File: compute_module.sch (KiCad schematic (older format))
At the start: 22 parts, among them Q1 2N7002P.215

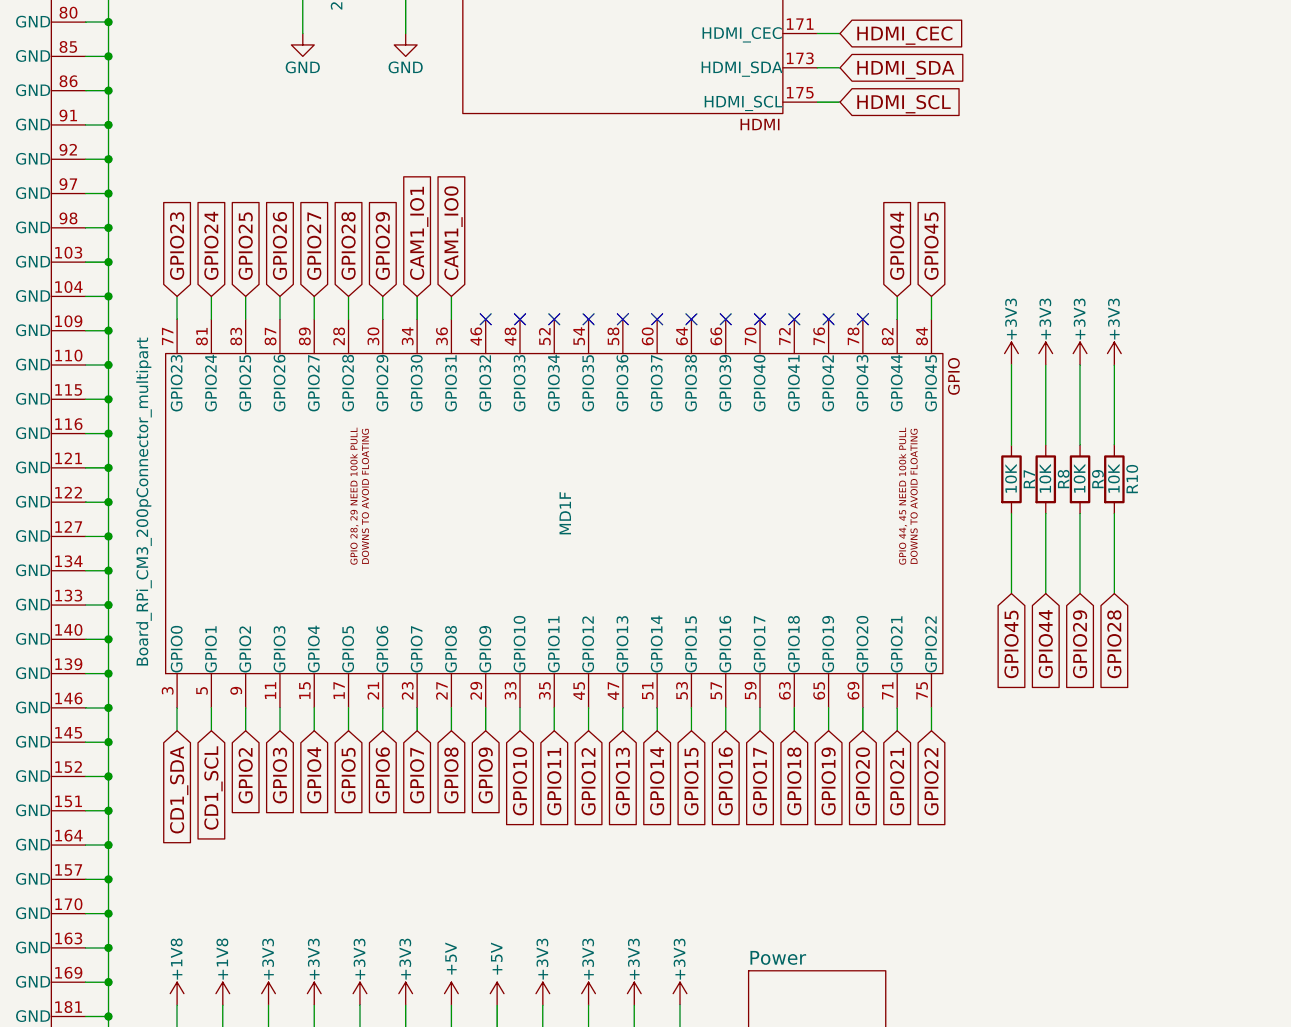
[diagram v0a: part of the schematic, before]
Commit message: Moved camera sda and scl to gpio 28 and 29
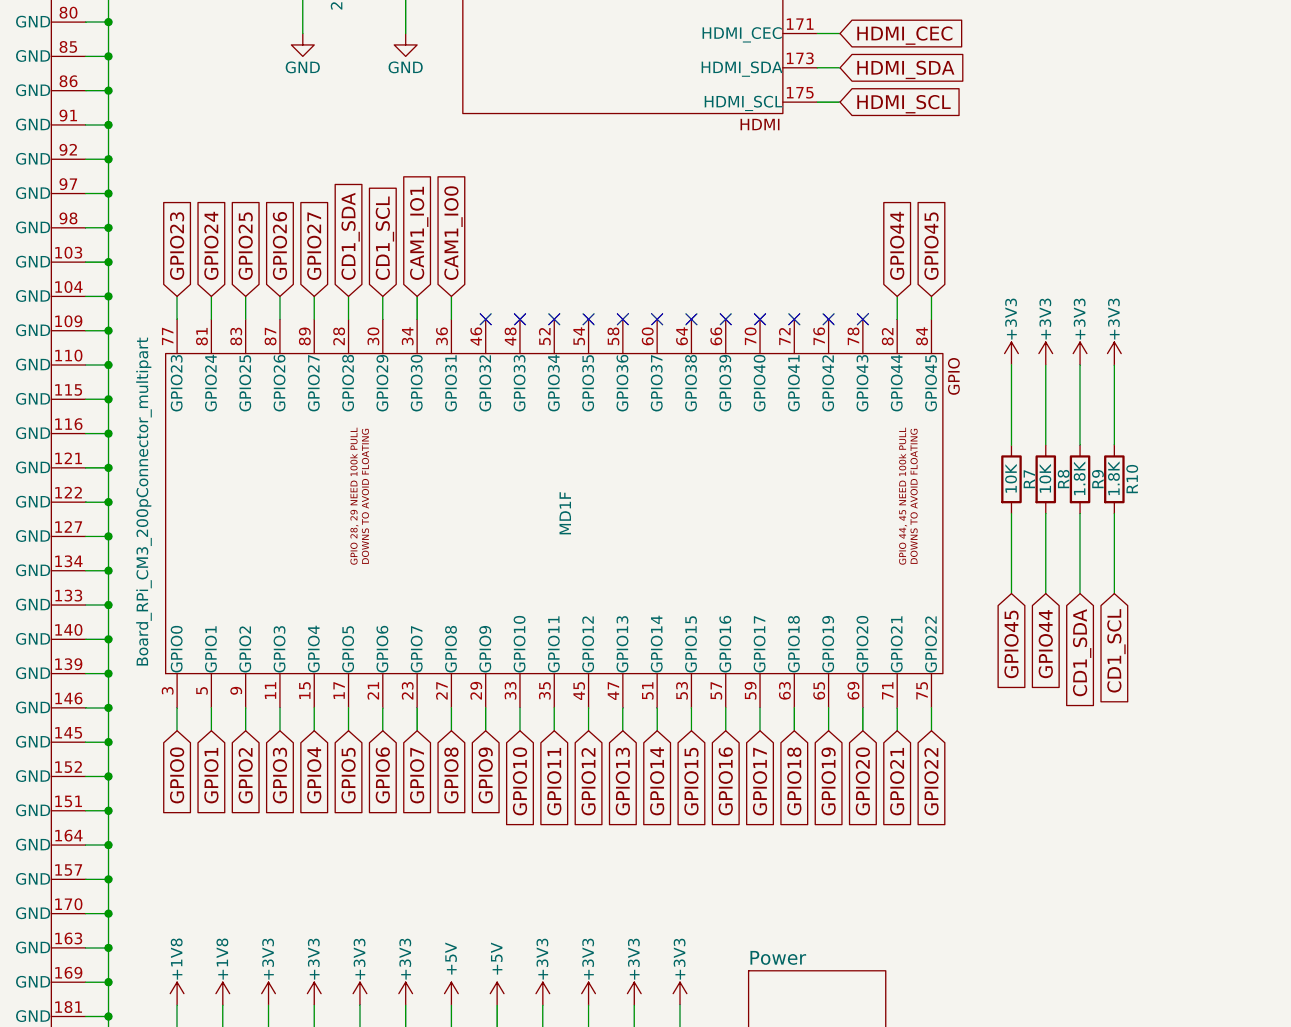
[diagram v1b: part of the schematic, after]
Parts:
- R10, R9: value 10K -> 1.8K
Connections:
- net CD1_SCL: now also MD1.30 (GPIO29), R10.2; no longer MD1.5 (GPIO1)
- net CD1_SDA: now also MD1.28 (GPIO28), R9.2; no longer MD1.3 (GPIO0)
- removed net GPIO28: MD1.28 (GPIO28), R10.2
- removed net GPIO29: MD1.30 (GPIO29), R9.2
- new net GPIO0: MD1.3 (GPIO0)
- new net GPIO1: MD1.5 (GPIO1)
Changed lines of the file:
@@
 NoConn ~ 9150 900
 NoConn ~ 9150 750
-Text GLabel 3550 5450 3    60   Input ~ 0
+Text GLabel 4300 3550 1    60   Input ~ 0
 CD1_SDA
-Text GLabel 3700 5450 3    60   Input ~ 0
+Text GLabel 4450 3550 1    60   Input ~ 0
 CD1_SCL
 Text GLabel 4600 3550 1    60   Input ~ 0
@@
 	1    0    0    -1
 $EndComp
-Text GLabel 4300 3550 1    60   Input ~ 0
-GPIO28
-Text GLabel 4450 3550 1    60   Input ~ 0
-GPIO29
 Text GLabel 6700 3550 1    60   Input ~ 0
 GPIO44
 Text GLabel 6850 3550 1    60   Input ~ 0
 GPIO45
-Text GLabel 7650 4850 3    60   Input ~ 0
-GPIO28
-Text GLabel 7500 4850 3    60   Input ~ 0
-GPIO29
 Text GLabel 7350 4850 3    60   Input ~ 0
 GPIO44
@@
 P 7500 4350
 F 0 "R9" V 7580 4350 50  0000 C CNN
-F 1 "10K" V 7500 4350 50  0000 C CNN
+F 1 "1.8K" V 7500 4350 50  0000 C CNN
 F 2 "Resistors_SMD:R_0603_HandSoldering" V 7430 4350 50  0001 C CNN
 F 3 "" H 7500 4350 50  0000 C CNN
@@
 P 7650 4350
 F 0 "R10" V 7730 4350 50  0000 C CNN
-F 1 "10K" V 7650 4350 50  0000 C CNN
+F 1 "1.8K" V 7650 4350 50  0000 C CNN
 F 2 "Resistors_SMD:R_0603_HandSoldering" V 7580 4350 50  0001 C CNN
 F 3 "" H 7650 4350 50  0000 C CNN
@@
 Text GLabel 4150 3550 1    60   Input ~ 0
 GPIO27
+Text GLabel 7500 4850 3    60   Input ~ 0
+CD1_SDA
+Text GLabel 7650 4850 3    60   Input ~ 0
+CD1_SCL
+Text GLabel 3550 5450 3    60   Input ~ 0
+GPIO0
+Text GLabel 3700 5450 3    60   Input ~ 0
+GPIO1
 $EndSCHEMATC

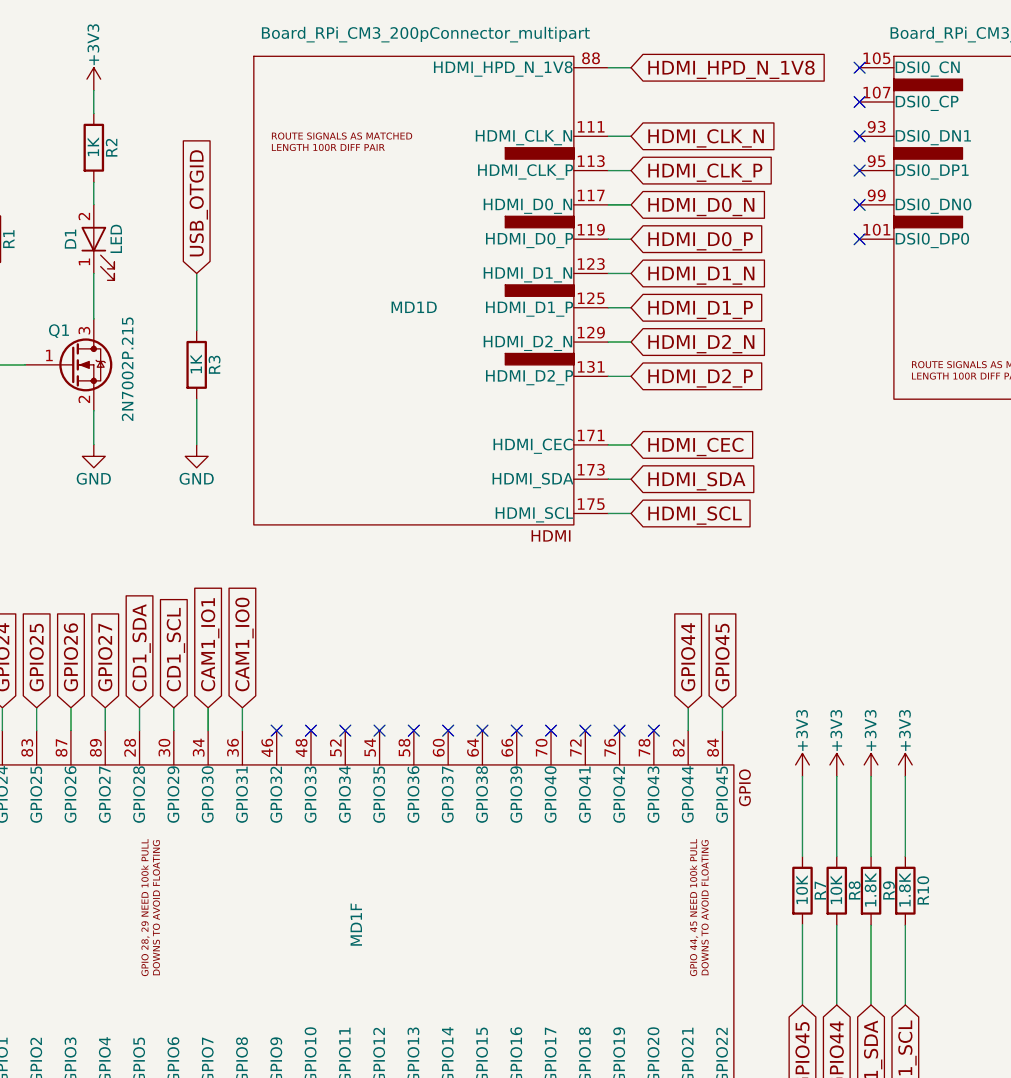
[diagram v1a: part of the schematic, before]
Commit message: Added power LED
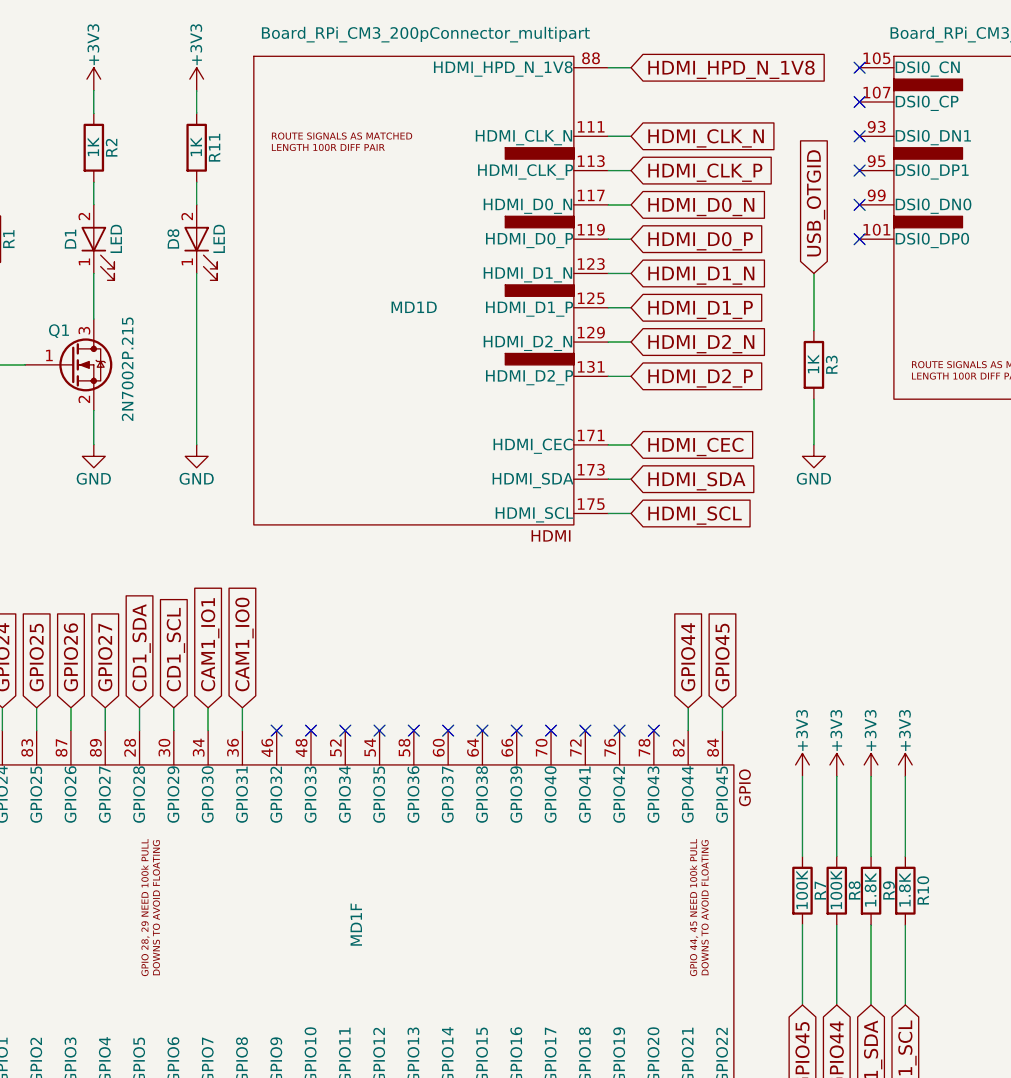
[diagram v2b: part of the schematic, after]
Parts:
- added D8: LED, LEDs:LED_0805, symbol LED
- added R11: 1K, Resistors_SMD:R_0603_HandSoldering, symbol R
- R7, R8: value 10K -> 100K
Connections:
- net +3V3: now also R11.1
- net GND: now also D8.1 (K)
- new net: D8.2 (A), R11.2
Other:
- moved on the sheet: R3

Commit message: Minor fixes
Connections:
- net +3V3: no longer R7.1, R8.1
- net GND: now also R7.2, R8.2
- net GPIO44: now also R8.1; no longer R8.2
- net GPIO45: now also R7.1; no longer R7.2
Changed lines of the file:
@@
 Text GLabel 6850 3550 1    60   Input ~ 0
 GPIO45
-Text GLabel 7350 4850 3    60   Input ~ 0
+Text GLabel 7350 3850 1    60   Input ~ 0
 GPIO44
-Text GLabel 7200 4850 3    60   Input ~ 0
+Text GLabel 7200 3850 1    60   Input ~ 0
 GPIO45
 $Comp
@@
 F 3 "" H 7650 4350 50  0000 C CNN
 	1    7650 4350
-	1    0    0    -1
-$EndComp
-$Comp
-L +3V3 #PWR36
-U 1 1 5C19C2CD
-P 7200 3850
-F 0 "#PWR36" H 7200 3700 50  0001 C CNN
-F 1 "+3V3" V 7200 4050 50  0000 C CNN
-F 2 "" H 7200 3850 50  0000 C CNN
-F 3 "" H 7200 3850 50  0000 C CNN
-	1    7200 3850
-	1    0    0    -1
-$EndComp
-$Comp
-L +3V3 #PWR38
-U 1 1 5C19C3B8
-P 7350 3850
-F 0 "#PWR38" H 7350 3700 50  0001 C CNN
-F 1 "+3V3" V 7350 4050 50  0000 C CNN
-F 2 "" H 7350 3850 50  0000 C CNN
-F 3 "" H 7350 3850 50  0000 C CNN
-	1    7350 3850
 	1    0    0    -1
 $EndComp
@@
 Wire Wire Line
 	4550 1650 4550 2400
+$Comp
+L GND #PWR?
+U 1 1 5C1D87F3
+P 7200 4850
+F 0 "#PWR?" H 7200 4600 50  0001 C CNN
+F 1 "GND" H 7200 4700 50  0000 C CNN
+F 2 "" H 7200 4850 50  0000 C CNN
+F 3 "" H 7200 4850 50  0000 C CNN
+	1    7200 4850
+	1    0    0    -1
+$EndComp
+$Comp
+L GND #PWR?
+U 1 1 5C1D8894
+P 7350 4850
+F 0 "#PWR?" H 7350 4600 50  0001 C CNN
+F 1 "GND" H 7350 4700 50  0000 C CNN
+F 2 "" H 7350 4850 50  0000 C CNN
+F 3 "" H 7350 4850 50  0000 C CNN
+	1    7350 4850
+	1    0    0    -1
+$EndComp
 $EndSCHEMATC
